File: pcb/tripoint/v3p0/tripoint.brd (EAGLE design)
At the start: 7.1 x 6.9 mm, 19 parts, among them IC1 ATMEGA325P, IC2 LM340MP-05, J1 DCJ0202

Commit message: added board layout for TriPoint
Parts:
- removed C1: 220nF, rcl:C0805
- removed C2: 100nF, rcl:C0805
- removed C3, C4, C5, C6, C7: 100nF, rcl:C0603
- removed IC1: ATMEGA325P, atmel:64M1
- removed IC2: LM340MP-05, linear:SOT223
- removed J1: DCJ0202, con-jack:DCJ0202
- removed LED1, LED2: GREEN, led:CHIP-LED0603
- removed QF1: 16M20AUM1, crystal:UM1
- removed R1: 10k, rcl:R0603
- removed R2, R3: 150, rcl:R0603
- removed S1: (no value), switch-omron:B3F-10XX
- removed SV1: (no value), con-lstb:MA03-2
- removed SV2: (no value), con-lstb:MA08-1
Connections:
- removed net +3V3: C2.1, C4.1, C5.1, IC1.15, IC1.4, IC2.3, R1.2, R2.2, SV1.5
- removed net GND: C1.2, C2.2, C3.2, C4.2, C5.2, C6.2, C7.2, IC1.16, IC1.22, IC1.53, IC1.8, IC2.4, J1.2, J1.3, LED1.C, LED2.C, S1.3, S1.4, SV1.1
- removed net MISO: IC1.32, SV1.6
- removed net MOSI: IC1.30, SV1.3
- removed net N$1: C1.1, IC2.1, J1.1
- removed net N$12: IC1.62, SV2.3
- removed net N$13: IC1.61, SV2.4
- removed net N$14: IC1.60, SV2.5
- removed net N$15: IC1.59, SV2.6
- removed net N$16: IC1.58, SV2.7
- removed net N$17: IC1.57, SV2.8
- removed net N$2: C3.1, IC1.5
- removed net N$3: C6.1, IC1.48, QF1.3
- removed net N$4: C7.1, IC1.47, QF1.1
- removed net N$5: IC1.64, SV2.1
- removed net N$6: LED1.A, R2.1
- removed net N$7: IC1.63, SV2.2
- removed net N$8: LED2.A, R3.1
- removed net RESET: IC1.17, R1.1, S1.1, S1.2, SV1.2
- removed net SCK: IC1.31, R3.2, SV1.4
- removed net VCC: IC1.21, IC1.52
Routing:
- net N$5: track 35.7 -> 0.00 mm
- net N$17: track 28.1 -> 0.00 mm
- net N$16: track 22.1 -> 0.00 mm
- net N$15: track 21.2 -> 0.00 mm
- net N$14: track 20.4 -> 0.00 mm
- net N$7: track 18.7 -> 0.00 mm, vias 2 -> 0
- net N$2: track 18.3 -> 0.00 mm
- net GND: track 15.5 -> 0.00 mm
- net +3V3: track 12.5 -> 0.00 mm
- net N$8: track 2.54 -> 0.00 mm
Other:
- board size 7.1 x 6.9 mm -> 31.8 x 27.5 mm
- board text added: "09/07/2018"
- board text added: "Andreas Biri"

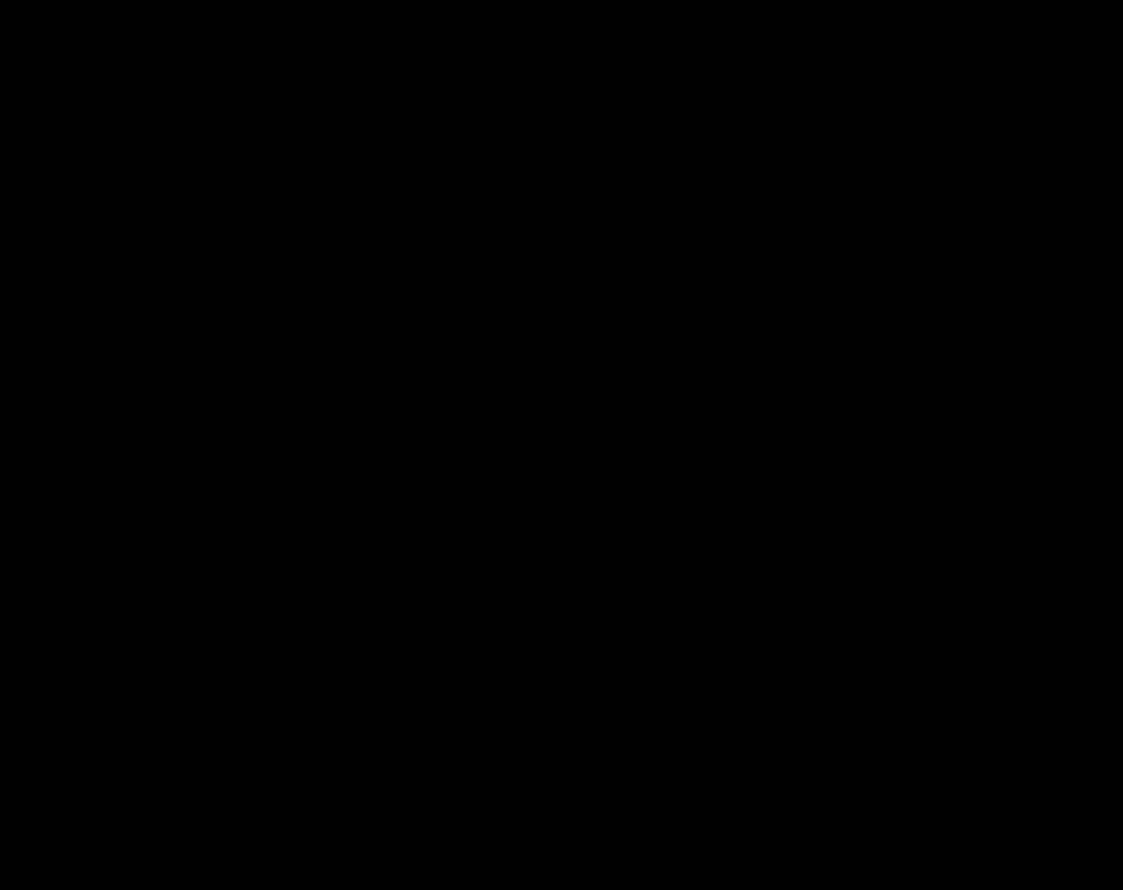
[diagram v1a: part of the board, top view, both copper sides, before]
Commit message: populated schematic without STM connections
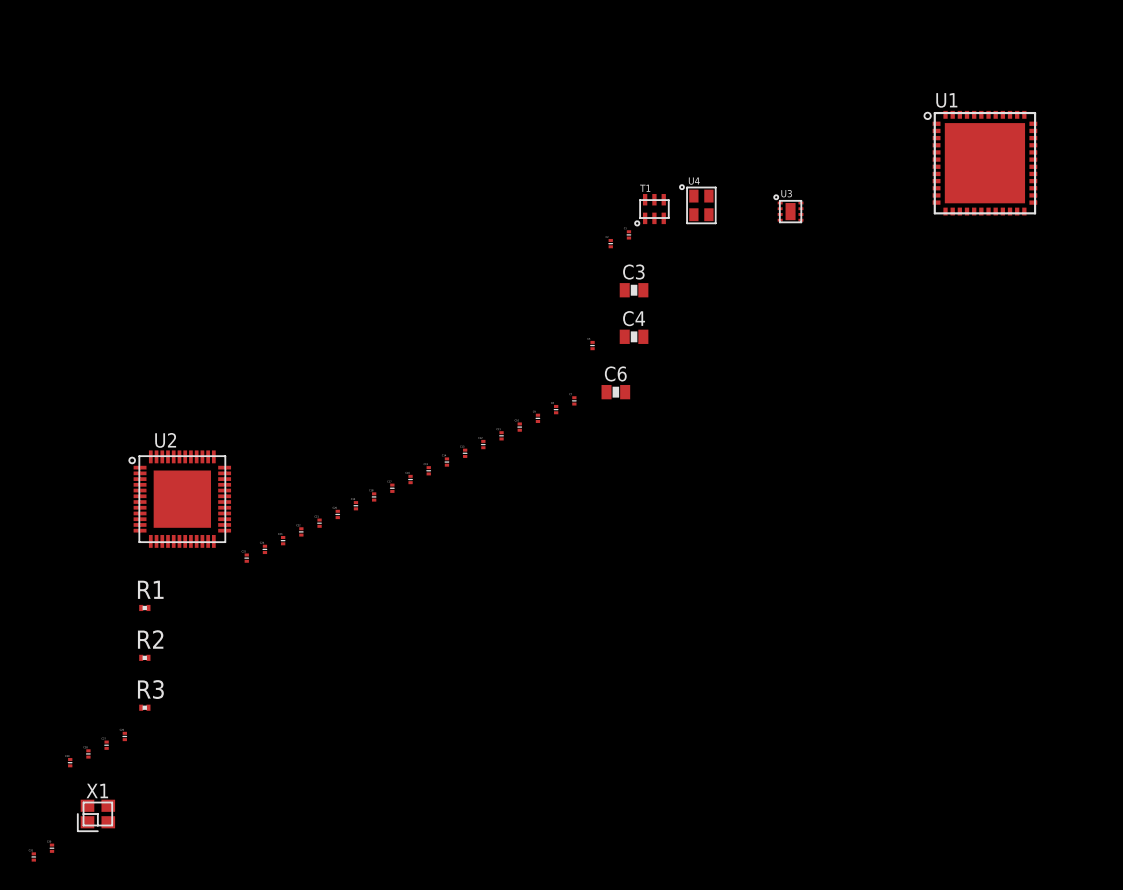
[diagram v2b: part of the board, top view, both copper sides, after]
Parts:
- added C1, C2, C30, C31: 12pF, passives:0201_CAP
- added C10, C11, C12, C13, C14, C15, C21, C22, C23, C24, C25, C5, C7, C9: 0.1uF, passives:0201_CAP
- added C16, C17: 10pF, passives:0201_CAP
- added C18, C19: 330pF, passives:0201_CAP
- added C20: 0.01uF, passives:0201_CAP
- added C26: 820pF, passives:0201_CAP
- added C27: 27pF, passives:0201_CAP
- added C28: 1.2pF, passives:0201_CAP
- added C29: 18pF, passives:0201_CAP
- added C3, C6: 4.7uF, passives:0603_CAP
- added C4: 10uF, passives:0603_CAP
- added C8: 100pF, passives:0201_CAP
- added R1: 270, rcl:R0201
- added R2: 16k, rcl:R0201
- added R3: 11k, rcl:R0201
- added T1: HHM1595A1, rf:EIA-0805
- added U1: STM32F091CC, chips:UFQFPN-48
- added U2: DW1000, chips:QFN-48-DW1000
- added U3: SKY13317, switches:MLPQ-UT-8
- added U4: LXDC2HN18A, regulators:LXDC2HN
- added X1: FA-128, crystals:FA-128
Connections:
- new net !DW_RST: U2.27
- new net !SPI_CS: U2.24
- new net ANT_SEL1: U3.3
- new net ANT_SEL2: U3.6
- new net ANT_SEL3: U3.7
- new net DW_IRQ: U2.45
- new net DW_SYNC: U2.29
- new net DW_WAKEUP: U2.23
- new net GND: C10.P$2, C11.P$2, C12.P$2, C13.P$2, C14.P$2, C15.P$2, C16.P$2, C17.P$2, C18.P$2, C19.P$2, C20.P$2, C21.P$2, C22.P$2, C23.P$2, C24.P$2, C25.P$2, C26.P$2, C27.P$2, C28.P$2, C29.P$2, C3.1, C30.P$2, C31.P$2, C4.2, C5.P$2, C6.2, C7.P$2, C8.P$2, C9.P$2, R3.1, T1.2, T1.5, U1.GND, U2.22, U2.32, U2.43, U2.46, U2.GND, U3.GND, U4.4, X1.2, X1.4
- new net N$1: T1.1, U3.1
- new net N$2: C1.P$2, T1.3
- new net N$3: C2.P$2, T1.4
- new net N$4: C26.P$1, R1.2
- new net N$5: C27.P$1, R2.2
- new net N$6: C29.P$1, R1.1, U2.12
- new net N$7: R3.2, U2.5
- new net N$9: C28.P$1, R2.1, U2.8
- new net RF1: U3.4
- new net RF2: U3.5
- new net RF3: U3.8
- new net RF_N: C1.P$1, U2.17
- new net RF_P: C2.P$1, U2.16
- new net SPI_CLK: U2.41
- new net SPI_MISO: U2.40
- new net SPI_MOSI: U2.39
- new net V1P8: C4.1, C5.P$1, C6.1, C9.P$1, U2.26, U2.48, U4.3
- new net V1P8_EN: U2.21, U4.2
- new net V3P3: C16.P$1, C17.P$1, C18.P$1, C19.P$1, C20.P$1, C21.P$1, C22.P$1, C23.P$1, C24.P$1, C25.P$1, C3.2, U2.15, U2.18, U2.19, U2.25, U2.28, U2.47, U4.1
- new net VBAT: U1.1
- new net VDD/24: U1.24
- new net VDD/48: U1.48
- new net VDDA: U1.9
- new net VDDCLK: C11.P$1, U2.9
- new net VDDDIG: C7.P$1, C8.P$1, U2.20, U2.44
- new net VDDIF: C14.P$1, U2.7
- new net VDDIO: C13.P$1, U2.31, U2.42
- new net VDDIO2: U1.36
- new net VDDMS: C10.P$1, U2.6
- new net VDDSYN: C12.P$1, U2.10
- new net VDDVCO: C15.P$1, U2.11
- new net VSS/23: U1.23
- new net VSS/35: U1.35
- new net VSS/47: U1.47
- new net VSSA: U1.8
- new net XTAL1: C31.P$1, U2.3, X1.3
- new net XTAL2: C30.P$1, U2.4, X1.1

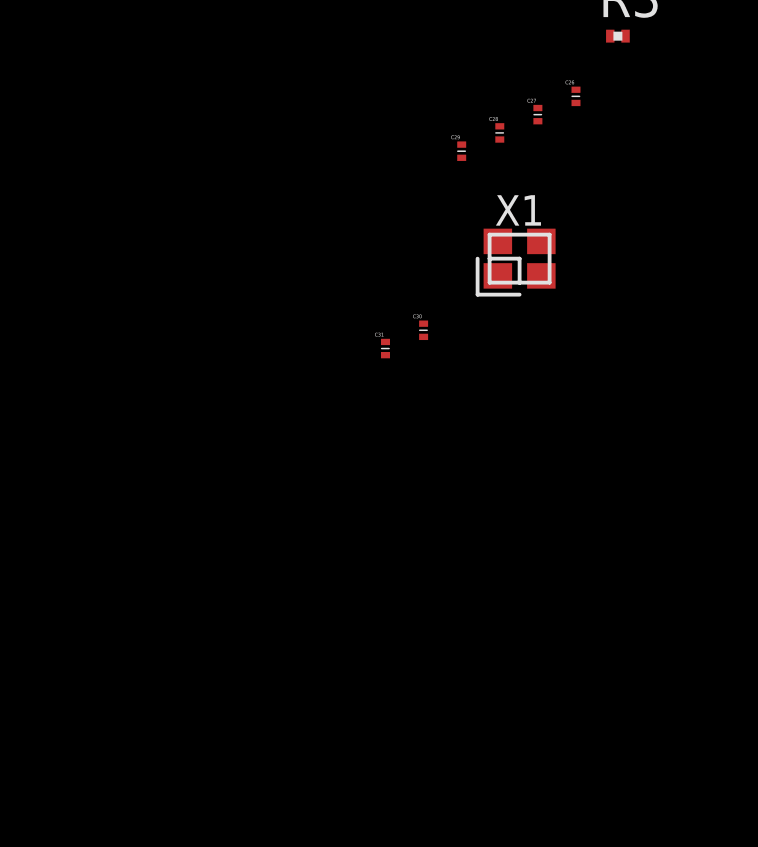
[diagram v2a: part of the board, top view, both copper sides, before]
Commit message: added oscillators
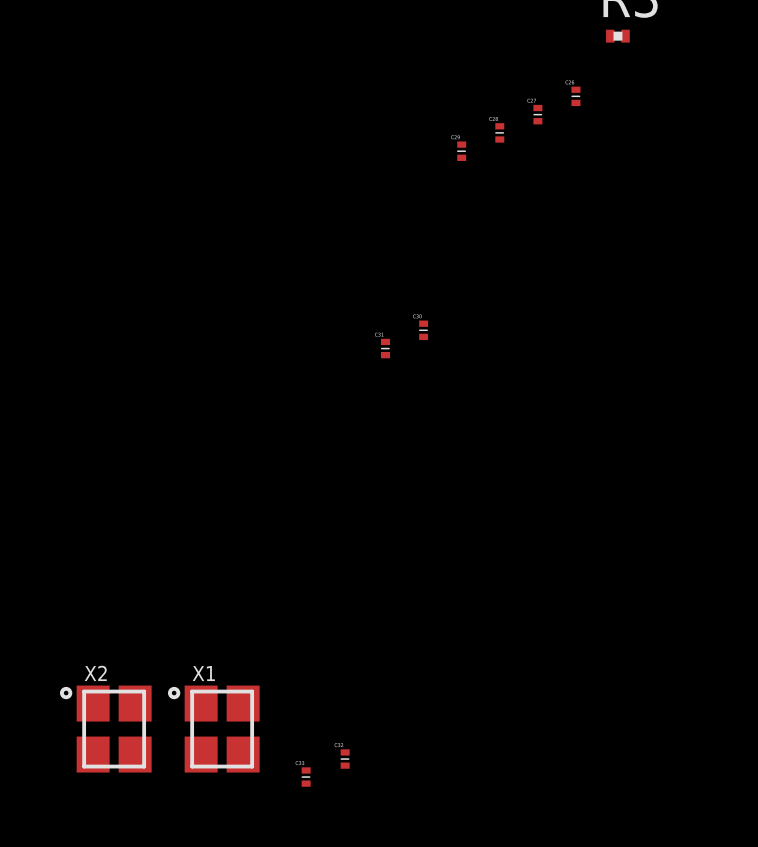
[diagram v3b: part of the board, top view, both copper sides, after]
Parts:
- added C32, C33: 8pF, passives:0201_CAP
- added X2: 16M, crystals:FA-20H
- C30, C31: value 12pF -> 8.5pF
- X1: value FA-128 -> 38.4M; device crystals:FA-128 -> crystals:FA-20H
- moved X1 18.6 mm to (-91.5, -74.1)
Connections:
- new net OSC_IN: C32.P$1, U1.5, X2.1
- new net OSC_OUT: C33.P$1, U1.6, X2.3
- net GND: now also C32.P$2, C33.P$2, X2.2, X2.4
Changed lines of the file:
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@@
 <setting verticaltext="up"/>
 </settings>
-<grid distance="1" unitdist="mil" unit="mil" style="lines" multiple="1" display="yes" altdistance="0.1" altunitdist="mil" altunit="mil"/>
+<grid distance="0.1" unitdist="mm" unit="mm" style="lines" multiple="1" display="yes" altdistance="0.01" altunitdist="mm" altunit="mm"/>
 <layers>
 <layer number="1" name="Top" color="4" fill="1" visible="yes" active="yes"/>
@@
 <element name="C28" library="passives" package="0201_CAP" value="1.2pF" x="-82.2452" y="-54.229"/>
 <element name="C29" library="passives" package="0201_CAP" value="18pF" x="-83.5152" y="-54.8386"/>
-<element name="X1" library="crystals" package="FA-128" value="FA-128" x="-81.5848" y="-58.42"/>
-<element name="C30" library="passives" package="0201_CAP" value="12pF" x="-84.7852" y="-60.8076"/>
-<element name="C31" library="passives" package="0201_CAP" value="12pF" x="-86.0552" y="-61.4172"/>
+<element name="C30" library="passives" package="0201_CAP" value="8.5pF" x="-84.7852" y="-60.8076"/>
+<element name="C31" library="passives" package="0201_CAP" value="8.5pF" x="-86.0552" y="-61.4172"/>
+<element name="C32" library="passives" package="0201_CAP" value="8pF" x="-87.4" y="-75.1"/>
+<element name="C33" library="passives" package="0201_CAP" value="8pF" x="-88.7" y="-75.7"/>
+<element name="X1" library="crystals" package="FA-20H" value="38.4M" x="-91.5" y="-74.1">
+<attribute name="DATASHEET" value="https://support.epson.biz/td/api/doc_check.php?dl=brief_FA-20H_en.pdf" x="-91.5" y="-74.1" size="1.778" layer="27" display="off"/>
+<attribute name="DESCRIPTION" value="38.4MHz ±10ppm Crystal 8.5pF 40 Ohms 4-SMD, No Lead" x="-91.5" y="-74.1" size="1.778" layer="27" display="off"/>
+<attribute name="DIGIKEY" value="SER3631CT-ND" x="-91.5" y="-74.1" size="1.778" layer="27" display="off"/>
+<attribute name="MANUFACTURER" value="EPSON" x="-91.5" y="-74.1" size="1.778" layer="27" display="off"/>
+</element>
+<element name="X2" library="crystals" package="FA-20H" value="16M" x="-95.1" y="-74.1">
+<attribute name="DATASHEET" value="https://support.epson.biz/td/api/doc_check.php?dl=brief_FA-20H_en.pdf" x="-95.1" y="-74.1" size="1.778" layer="27" display="off"/>
+<attribute name="DESCRIPTION" value="16MHz ±10ppm Crystal 8pF 80 Ohms 4-SMD, No Lead" x="-95.1" y="-74.1" size="1.778" layer="27" display="off"/>
+<attribute name="DIGIKEY" value="SER3913CT-ND" x="-95.1" y="-74.1" size="1.778" layer="27" display="off"/>
+<attribute name="MANUFACTURER" value="EPSON" x="-95.1" y="-74.1" size="1.778" layer="27" display="off"/>
+</element>
 </elements>
 <signals>
@@
 <contactref element="U2" pad="43"/>
 <contactref element="R3" pad="1"/>
+<contactref element="U2" pad="46"/>
+<contactref element="U2" pad="22"/>
 <contactref element="C30" pad="P$2"/>
 <contactref element="C31" pad="P$2"/>
 <contactref element="X1" pad="2"/>
 <contactref element="X1" pad="4"/>
-<contactref element="U2" pad="46"/>
-<contactref element="U2" pad="22"/>
-<wire x1="-86.0552" y1="-61.6372" x2="-84.7852" y2="-61.0276" width="0" layer="19" extent="1-1"/>
-<wire x1="-82.3098" y1="-57.845" x2="-84.7852" y2="-61.0276" width="0" layer="19" extent="1-1"/>
-<wire x1="-80.8598" y1="-58.995" x2="-82.3098" y2="-57.845" width="0" layer="19" extent="1-1"/>
-<wire x1="-83.5152" y1="-55.0586" x2="-82.3098" y2="-57.845" width="0" layer="19" extent="1-1"/>
+<contactref element="C32" pad="P$2"/>
+<contactref element="C33" pad="P$2"/>
+<contactref element="X2" pad="2"/>
+<contactref element="X2" pad="4"/>
+<wire x1="-94.4" y1="-73.25" x2="-95.8" y2="-74.95" width="0" layer="19" extent="1-1"/>
+<wire x1="-92.2" y1="-74.95" x2="-94.4" y2="-73.25" width="0" layer="19" extent="1-1"/>
+<wire x1="-90.8" y1="-73.25" x2="-92.2" y2="-74.95" width="0" layer="19" extent="1-1"/>
+<wire x1="-88.7" y1="-75.92" x2="-90.8" y2="-73.25" width="0" layer="19" extent="1-1"/>
+<wire x1="-87.4" y1="-75.32" x2="-88.7" y2="-75.92" width="0" layer="19" extent="1-1"/>
+<wire x1="-86.0552" y1="-61.6372" x2="-90.8" y2="-73.25" width="0" layer="19" extent="1-1"/>
+<wire x1="-84.7852" y1="-61.0276" x2="-86.0552" y2="-61.6372" width="0" layer="19" extent="1-1"/>
+<wire x1="-83.5152" y1="-55.0586" x2="-84.7852" y2="-61.0276" width="0" layer="19" extent="1-1"/>
 <wire x1="-82.2452" y1="-54.449" x2="-83.5152" y2="-55.0586" width="0" layer="19" extent="1-1"/>
 <wire x1="-80.9752" y1="-53.8394" x2="-82.2452" y2="-54.449" width="0" layer="19" extent="1-1"/>
@@
 </signal>
 <signal name="XTAL2">
-<contactref element="X1" pad="1"/>
 <contactref element="C30" pad="P$1"/>
 <contactref element="U2" pad="4"/>
-<wire x1="-82.3098" y1="-58.995" x2="-84.7852" y2="-60.5876" width="0" layer="19" extent="1-1"/>
-<wire x1="-78.642" y1="-35.449" x2="-82.3098" y2="-58.995" width="0" layer="19" extent="1-1"/>
+<contactref element="X1" pad="1"/>
+<wire x1="-84.7852" y1="-60.5876" x2="-92.2" y2="-73.25" width="0" layer="19" extent="1-1"/>
+<wire x1="-78.642" y1="-35.449" x2="-84.7852" y2="-60.5876" width="0" layer="19" extent="1-1"/>
 </signal>
 <signal name="XTAL1">
-<contactref element="X1" pad="3"/>
 <contactref element="C31" pad="P$1"/>
 <contactref element="U2" pad="3"/>
-<wire x1="-80.8598" y1="-57.845" x2="-86.0552" y2="-61.1972" width="0" layer="19" extent="1-1"/>
-<wire x1="-78.642" y1="-35.049" x2="-80.8598" y2="-57.845" width="0" layer="19" extent="1-1"/>
+<contactref element="X1" pad="3"/>
+<wire x1="-86.0552" y1="-61.1972" x2="-90.8" y2="-74.95" width="0" layer="19" extent="1-1"/>
+<wire x1="-78.642" y1="-35.049" x2="-86.0552" y2="-61.1972" width="0" layer="19" extent="1-1"/>
 </signal>
 <signal name="DW_WAKEUP">
@@
 <contactref element="U2" pad="45"/>
 </signal>
+<signal name="OSC_IN">
+<contactref element="C32" pad="P$1"/>
+<contactref element="U1" pad="5"/>
+<contactref element="X2" pad="1"/>
+<wire x1="-87.4" y1="-74.88" x2="-95.8" y2="-73.25" width="0" layer="19" extent="1-1"/>
+<wire x1="-23.06" y1="-12.2548" x2="-87.4" y2="-74.88" width="0" layer="19" extent="1-1"/>
+</signal>
+<signal name="OSC_OUT">
+<contactref element="C33" pad="P$1"/>
+<contactref element="U1" pad="6"/>
+<contactref element="X2" pad="3"/>
+<wire x1="-88.7" y1="-75.48" x2="-94.4" y2="-74.95" width="0" layer="19" extent="1-1"/>
+<wire x1="-23.06" y1="-12.7548" x2="-88.7" y2="-75.48" width="0" layer="19" extent="1-1"/>
+</signal>
 </signals>
